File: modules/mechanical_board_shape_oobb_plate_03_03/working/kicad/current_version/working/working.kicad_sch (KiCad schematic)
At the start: 9 parts

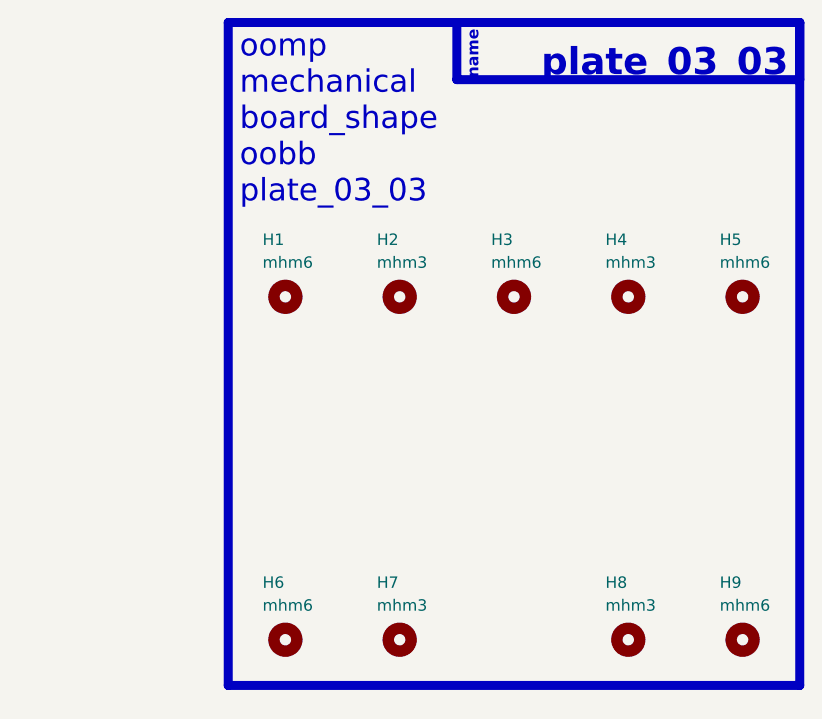
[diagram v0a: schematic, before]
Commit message: fixed formatting to be more consistent
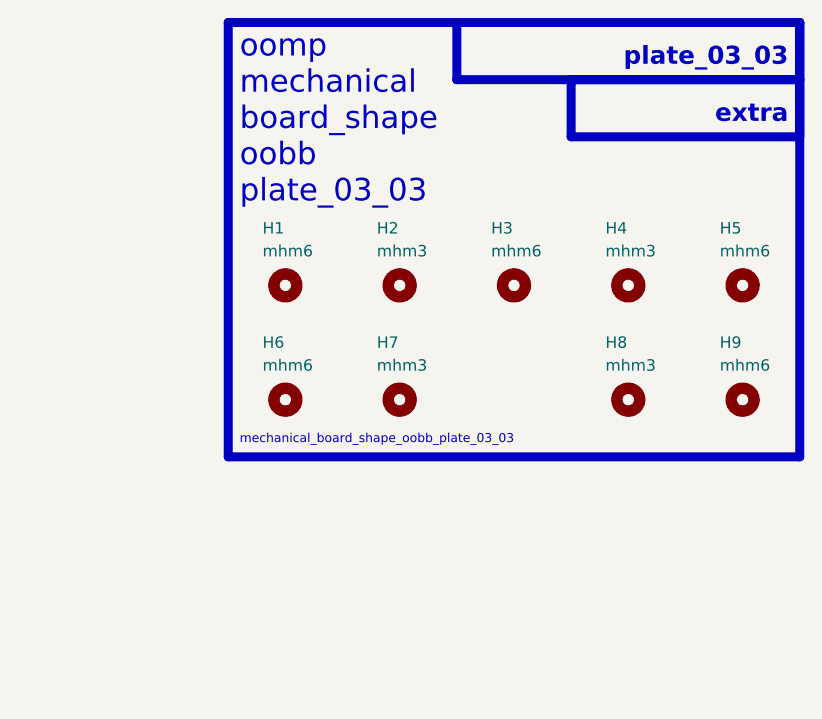
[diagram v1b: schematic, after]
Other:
- note added: "extra"
- note added: "mechanical_board_shape_oobb_plate_03_03"
- note removed: "name"
- moved on the sheet: H1, H2, H3, H4, H5, H6, H7, H8, H9

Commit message: schematic formatting
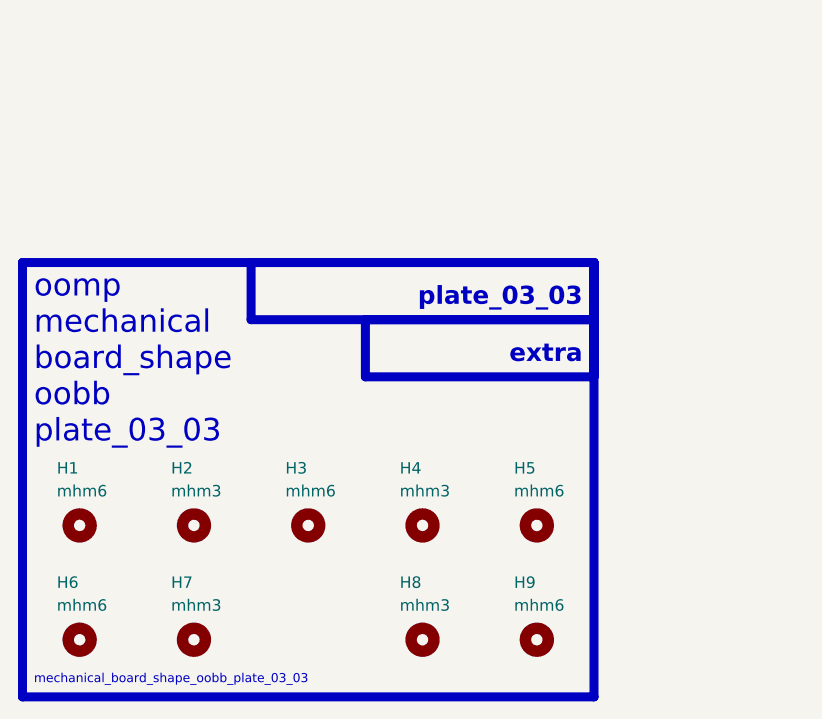
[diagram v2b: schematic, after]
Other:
- moved on the sheet: H1, H2, H3, H4, H5, H6, H7, H8, H9
